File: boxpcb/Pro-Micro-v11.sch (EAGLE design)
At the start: 30 parts

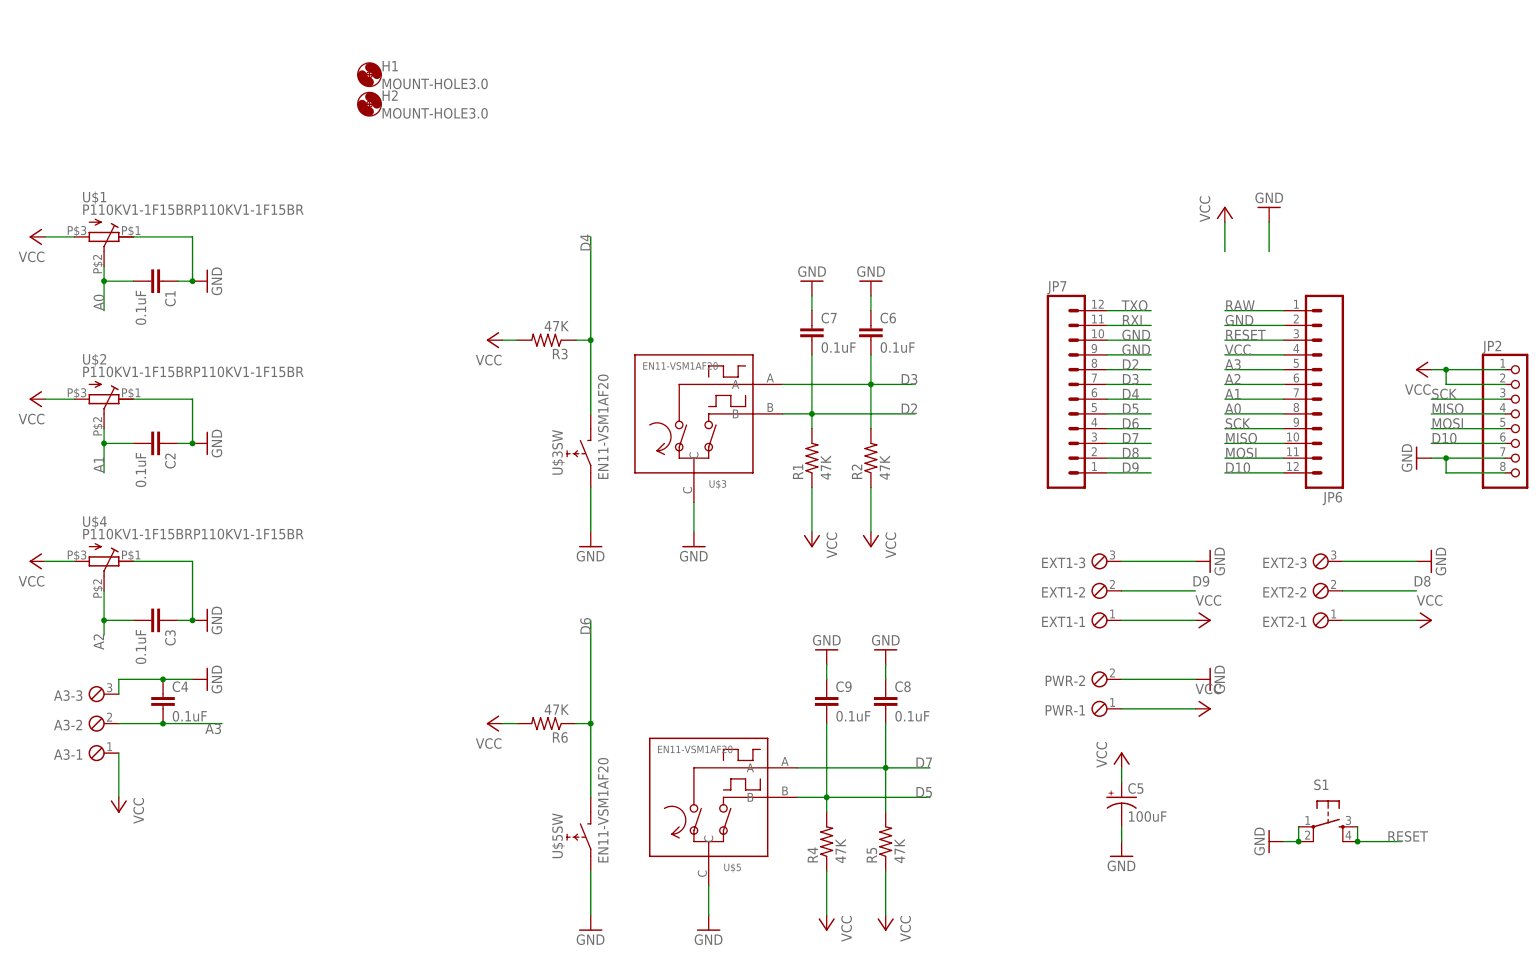
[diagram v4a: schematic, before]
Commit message: pcb simplification - remove dual rot/pot
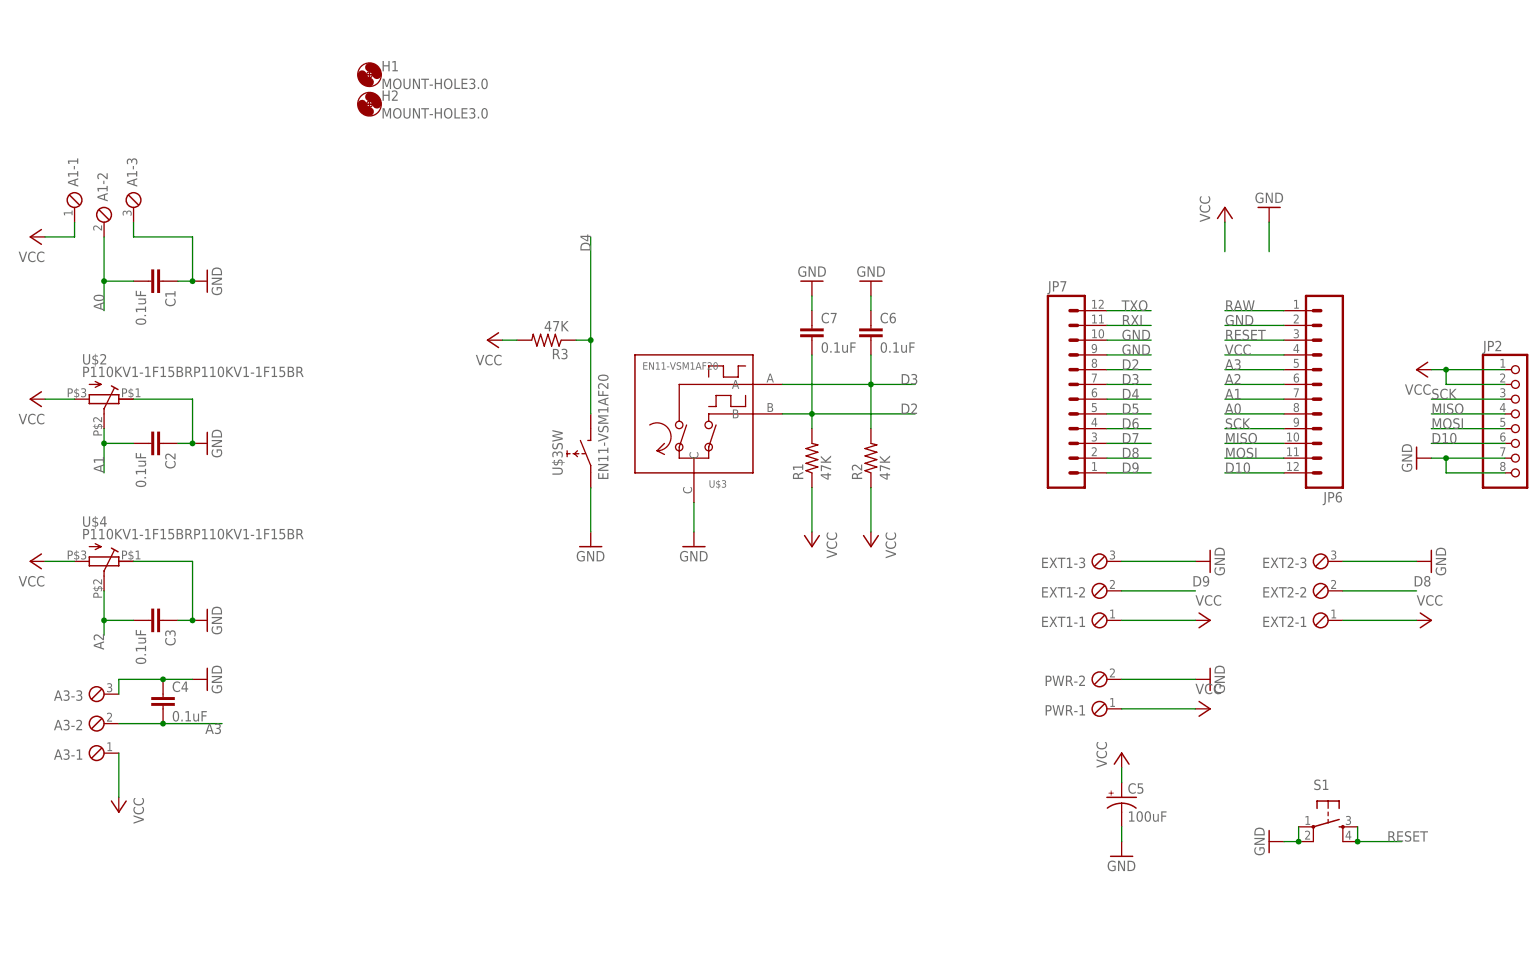
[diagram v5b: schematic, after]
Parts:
- removed C8, C9: 0.1uF, rcl:C-EU025-024X044
- removed R4, R5, R6: 47K, rcl:R-US_0204/5
- removed U$1: P110KV1-1F15BRP110KV1-1F15BR, keves:P110KV1-1F15BRP110KV1-1F15BR
- removed U$5: EN11-VSM1AF20, rotary-encoder:EN11
- added A1: (no value), con-phoenix-254:MPT3
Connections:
- net A0: now also A1-2.1; no longer U$1.S
- net D5: no longer C9.2, R4.2, U$5G$1.B
- net D6: no longer R6.1, U$5SW.E
- net D7: no longer C8.2, R5.2, U$5G$1.A
- net GND: now also A1-3.1; no longer C8.1, C9.1, U$1.A, U$5G$1.C, U$5SW.D
- net VCC: now also A1-1.1; no longer R4.1, R5.1, R6.2, U$1.E
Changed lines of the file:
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@@
 <part name="JP6" library="SparkFun" deviceset="M12" device="PTH" value=""/>
 <part name="JP7" library="SparkFun" deviceset="M12" device="PTH" value=""/>
-<part name="U$1" library="keves" deviceset="P110KV1-1F15BR" device="P110KV1-1F15BR"/>
 <part name="U$2" library="keves" deviceset="P110KV1-1F15BR" device="P110KV1-1F15BR"/>
 <part name="U$3" library="rotary-encoder" deviceset="EN11" device="" value="EN11-VSM1AF20"/>
@@
 <part name="R3" library="rcl" deviceset="R-US_" device="0204/5" value="47K"/>
 <part name="P+8" library="supply1" deviceset="VCC" device=""/>
-<part name="U$5" library="rotary-encoder" deviceset="EN11" device="" value="EN11-VSM1AF20"/>
-<part name="R4" library="rcl" deviceset="R-US_" device="0204/5" value="47K"/>
-<part name="R5" library="rcl" deviceset="R-US_" device="0204/5" value="47K"/>
-<part name="GND8" library="supply1" deviceset="GND" device=""/>
-<part name="P+9" library="supply1" deviceset="VCC" device=""/>
-<part name="P+10" library="supply1" deviceset="VCC" device=""/>
-<part name="GND9" library="supply1" deviceset="GND" device=""/>
-<part name="R6" library="rcl" deviceset="R-US_" device="0204/5" value="47K"/>
-<part name="P+11" library="supply1" deviceset="VCC" device=""/>
 <part name="EXT1" library="con-phoenix-254" deviceset="MPT3" device=""/>
 <part name="PWR" library="con-phoenix-254" deviceset="MPT2" device=""/>
@@
 <part name="C6" library="rcl" deviceset="C-EU" device="025-024X044" value="0.1uF"/>
 <part name="C7" library="rcl" deviceset="C-EU" device="025-024X044" value="0.1uF"/>
-<part name="C8" library="rcl" deviceset="C-EU" device="025-024X044" value="0.1uF"/>
-<part name="C9" library="rcl" deviceset="C-EU" device="025-024X044" value="0.1uF"/>
 <part name="GND14" library="supply1" deviceset="GND" device=""/>
 <part name="GND15" library="supply1" deviceset="GND" device=""/>
-<part name="GND16" library="supply1" deviceset="GND" device=""/>
-<part name="GND17" library="supply1" deviceset="GND" device=""/>
 <part name="S1" library="SparkFun-Electromechanical" deviceset="TAC_SWITCH" device="PTH"/>
 <part name="GND18" library="supply1" deviceset="GND" device=""/>
@@
 <part name="H1" library="holes" deviceset="MOUNT-HOLE" device="3.0"/>
 <part name="H2" library="holes" deviceset="MOUNT-HOLE" device="3.0"/>
+<part name="A1" library="con-phoenix-254" deviceset="MPT3" device=""/>
 </parts>
 <sheets>
@@
 <instance part="JP6" gate="G$1" x="241.3" y="147.32" rot="R180"/>
 <instance part="JP7" gate="G$1" x="190.5" y="149.86"/>
-<instance part="U$1" gate="G$1" x="27.94" y="175.26" rot="R270"/>
 <instance part="U$2" gate="G$1" x="27.94" y="147.32" rot="R270"/>
 <instance part="U$3" gate="G$1" x="129.54" y="144.78"/>
@@
 <instance part="R3" gate="G$1" x="104.14" y="157.48" rot="R180"/>
 <instance part="P+8" gate="VCC" x="93.98" y="157.48" rot="R90"/>
-<instance part="U$5" gate="G$1" x="132.08" y="78.74"/>
-<instance part="U$5" gate="SW" x="109.22" y="71.12" rot="R90"/>
-<instance part="R4" gate="G$1" x="152.4" y="71.12" rot="R90"/>
-<instance part="R5" gate="G$1" x="162.56" y="71.12" rot="R90"/>
-<instance part="GND8" gate="1" x="132.08" y="55.88"/>
-<instance part="P+9" gate="VCC" x="152.4" y="55.88" rot="R180"/>
-<instance part="P+10" gate="VCC" x="162.56" y="55.88" rot="R180"/>
-<instance part="GND9" gate="1" x="111.76" y="55.88"/>
-<instance part="R6" gate="G$1" x="104.14" y="91.44" rot="R180"/>
-<instance part="P+11" gate="VCC" x="93.98" y="91.44" rot="R90"/>
 <instance part="EXT1" gate="-1" x="200.66" y="109.22" rot="R180"/>
 <instance part="EXT1" gate="-2" x="200.66" y="114.3" rot="R180"/>
@@
 <instance part="C6" gate="G$1" x="160.02" y="160.02"/>
 <instance part="C7" gate="G$1" x="149.86" y="160.02"/>
-<instance part="C8" gate="G$1" x="162.56" y="96.52"/>
-<instance part="C9" gate="G$1" x="152.4" y="96.52"/>
 <instance part="GND14" gate="1" x="160.02" y="167.64" rot="R180"/>
 <instance part="GND15" gate="1" x="149.86" y="167.64" rot="R180"/>
-<instance part="GND16" gate="1" x="152.4" y="104.14" rot="R180"/>
-<instance part="GND17" gate="1" x="162.56" y="104.14" rot="R180"/>
 <instance part="S1" gate="S" x="238.76" y="73.66"/>
 <instance part="GND18" gate="1" x="228.6" y="71.12" rot="R270"/>
@@
 <instance part="H1" gate="G$1" x="73.66" y="203.2"/>
 <instance part="H2" gate="G$1" x="73.66" y="198.12"/>
+<instance part="A1" gate="-1" x="22.86" y="180.34" rot="R90"/>
+<instance part="A1" gate="-2" x="27.94" y="177.8" rot="R90"/>
+<instance part="A1" gate="-3" x="33.02" y="180.34" rot="R90"/>
 </instances>
 <busses>
@@
 <pinref part="C1" gate="G$1" pin="1"/>
 <wire x1="43.18" y1="167.64" x2="40.64" y2="167.64" width="0.1524" layer="91"/>
-<pinref part="U$1" gate="G$1" pin="A"/>
 <wire x1="33.02" y1="175.26" x2="43.18" y2="175.26" width="0.1524" layer="91"/>
 <wire x1="43.18" y1="175.26" x2="43.18" y2="167.64" width="0.1524" layer="91"/>
 <junction x="43.18" y="167.64"/>
+<pinref part="A1" gate="-3" pin="1"/>
+<wire x1="33.02" y1="175.26" x2="33.02" y2="177.8" width="0.1524" layer="91"/>
 </segment>
 <segment>
@@
 </segment>
 <segment>
-<pinref part="U$5" gate="G$1" pin="C"/>
-<pinref part="GND8" gate="1" pin="GND"/>
-<wire x1="132.08" y1="63.5" x2="132.08" y2="58.42" width="0.1524" layer="91"/>
-</segment>
-<segment>
-<pinref part="GND9" gate="1" pin="GND"/>
-<pinref part="U$5" gate="SW" pin="D"/>
-<wire x1="111.76" y1="58.42" x2="111.76" y2="66.04" width="0.1524" layer="91"/>
-</segment>
-<segment>
 <pinref part="PWR" gate="-2" pin="1"/>
 <wire x1="203.2" y1="99.06" x2="215.9" y2="99.06" width="0.1524" layer="91"/>
@@
 <pinref part="C5" gate="G$1" pin="-"/>
 <wire x1="203.2" y1="71.12" x2="203.2" y2="73.66" width="0.1524" layer="91"/>
-</segment>
-<segment>
-<pinref part="GND17" gate="1" pin="GND"/>
-<pinref part="C8" gate="G$1" pin="1"/>
-<wire x1="162.56" y1="101.6" x2="162.56" y2="99.06" width="0.1524" layer="91"/>
-</segment>
-<segment>
-<pinref part="GND16" gate="1" pin="GND"/>
-<pinref part="C9" gate="G$1" pin="1"/>
-<wire x1="152.4" y1="101.6" x2="152.4" y2="99.06" width="0.1524" layer="91"/>
 </segment>
 <segment>
@@
 </segment>
 <segment>
-<pinref part="U$1" gate="G$1" pin="E"/>
 <pinref part="P+1" gate="VCC" pin="VCC"/>
 <wire x1="22.86" y1="175.26" x2="17.78" y2="175.26" width="0.1524" layer="91"/>
+<pinref part="A1" gate="-1" pin="1"/>
+<wire x1="22.86" y1="177.8" x2="22.86" y2="175.26" width="0.1524" layer="91"/>
 </segment>
 <segment>
@@
 <pinref part="R3" gate="G$1" pin="2"/>
 <wire x1="99.06" y1="157.48" x2="96.52" y2="157.48" width="0.1524" layer="91"/>
-</segment>
-<segment>
-<pinref part="R4" gate="G$1" pin="1"/>
-<pinref part="P+9" gate="VCC" pin="VCC"/>
-<wire x1="152.4" y1="66.04" x2="152.4" y2="58.42" width="0.1524" layer="91"/>
-</segment>
-<segment>
-<pinref part="R5" gate="G$1" pin="1"/>
-<pinref part="P+10" gate="VCC" pin="VCC"/>
-<wire x1="162.56" y1="66.04" x2="162.56" y2="58.42" width="0.1524" layer="91"/>
-</segment>
-<segment>
-<pinref part="P+11" gate="VCC" pin="VCC"/>
-<pinref part="R6" gate="G$1" pin="2"/>
-<wire x1="99.06" y1="91.44" x2="96.52" y2="91.44" width="0.1524" layer="91"/>
 </segment>
 <segment>
@@
 </segment>
 <segment>
-<pinref part="U$1" gate="G$1" pin="S"/>
-<wire x1="27.94" y1="170.18" x2="27.94" y2="167.64" width="0.1524" layer="91"/>
 <label x="27.94" y="162.56" size="1.778" layer="95" rot="R90"/>
 <pinref part="C1" gate="G$1" pin="2"/>
@@
 <wire x1="33.02" y1="167.64" x2="27.94" y2="167.64" width="0.1524" layer="91"/>
 <junction x="27.94" y="167.64"/>
+<pinref part="A1" gate="-2" pin="1"/>
+<wire x1="27.94" y1="175.26" x2="27.94" y2="167.64" width="0.1524" layer="91"/>
 </segment>
 </net>
@@
 <pinref part="JP7" gate="G$1" pin="5"/>
 </segment>
-<segment>
-<pinref part="U$5" gate="G$1" pin="B"/>
-<pinref part="R4" gate="G$1" pin="2"/>
-<wire x1="147.32" y1="78.74" x2="152.4" y2="78.74" width="0.1524" layer="91"/>
-<wire x1="152.4" y1="78.74" x2="152.4" y2="76.2" width="0.1524" layer="91"/>
-<wire x1="152.4" y1="78.74" x2="170.18" y2="78.74" width="0.1524" layer="91"/>
-<junction x="152.4" y="78.74"/>
-<label x="167.64" y="78.74" size="1.778" layer="95"/>
-<pinref part="C9" gate="G$1" pin="2"/>
-<wire x1="152.4" y1="91.44" x2="152.4" y2="78.74" width="0.1524" layer="91"/>
-</segment>
 </net>
 <net name="D6" class="0">
@@
 <pinref part="JP7" gate="G$1" pin="4"/>
 </segment>
-<segment>
-<pinref part="U$5" gate="SW" pin="E"/>
-<wire x1="111.76" y1="78.74" x2="111.76" y2="91.44" width="0.1524" layer="91"/>
-<pinref part="R6" gate="G$1" pin="1"/>
-<wire x1="111.76" y1="91.44" x2="111.76" y2="109.22" width="0.1524" layer="91"/>
-<wire x1="111.76" y1="91.44" x2="109.22" y2="91.44" width="0.1524" layer="91"/>
-<junction x="111.76" y="91.44"/>
-<label x="111.76" y="106.68" size="1.778" layer="95" rot="R90"/>
-</segment>
 </net>
 <net name="D7" class="0">
@@
 <pinref part="JP7" gate="G$1" pin="3"/>
 </segment>
-<segment>
-<pinref part="U$5" gate="G$1" pin="A"/>
-<pinref part="R5" gate="G$1" pin="2"/>
-<wire x1="147.32" y1="83.82" x2="162.56" y2="83.82" width="0.1524" layer="91"/>
-<wire x1="162.56" y1="83.82" x2="162.56" y2="76.2" width="0.1524" layer="91"/>
-<wire x1="162.56" y1="83.82" x2="170.18" y2="83.82" width="0.1524" layer="91"/>
-<junction x="162.56" y="83.82"/>
-<label x="167.64" y="83.82" size="1.778" layer="95"/>
-<pinref part="C8" gate="G$1" pin="2"/>
-<wire x1="162.56" y1="91.44" x2="162.56" y2="83.82" width="0.1524" layer="91"/>
-</segment>
-</net>
+</net>

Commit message: wip
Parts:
- renumbered A1 to A2
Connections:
- net A0: now also C3.2, U$4.S; no longer A2-2.1, C1.2
- net A2: now also A2-2.1, C1.2; no longer C3.2, U$4.S
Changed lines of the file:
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@@
 <part name="H1" library="holes" deviceset="MOUNT-HOLE" device="3.0"/>
 <part name="H2" library="holes" deviceset="MOUNT-HOLE" device="3.0"/>
-<part name="A1" library="con-phoenix-254" deviceset="MPT3" device=""/>
+<part name="A2" library="con-phoenix-254" deviceset="MPT3" device=""/>
 </parts>
 <sheets>
@@
 <instance part="H1" gate="G$1" x="73.66" y="203.2"/>
 <instance part="H2" gate="G$1" x="73.66" y="198.12"/>
-<instance part="A1" gate="-1" x="22.86" y="180.34" rot="R90"/>
-<instance part="A1" gate="-2" x="27.94" y="177.8" rot="R90"/>
-<instance part="A1" gate="-3" x="33.02" y="180.34" rot="R90"/>
+<instance part="A2" gate="-1" x="22.86" y="180.34" rot="R90"/>
+<instance part="A2" gate="-2" x="27.94" y="177.8" rot="R90"/>
+<instance part="A2" gate="-3" x="33.02" y="180.34" rot="R90"/>
 </instances>
 <busses>
@@
 <wire x1="43.18" y1="175.26" x2="43.18" y2="167.64" width="0.1524" layer="91"/>
 <junction x="43.18" y="167.64"/>
-<pinref part="A1" gate="-3" pin="1"/>
+<pinref part="A2" gate="-3" pin="1"/>
 <wire x1="33.02" y1="175.26" x2="33.02" y2="177.8" width="0.1524" layer="91"/>
 </segment>
@@
 <pinref part="P+1" gate="VCC" pin="VCC"/>
 <wire x1="22.86" y1="175.26" x2="17.78" y2="175.26" width="0.1524" layer="91"/>
-<pinref part="A1" gate="-1" pin="1"/>
+<pinref part="A2" gate="-1" pin="1"/>
 <wire x1="22.86" y1="177.8" x2="22.86" y2="175.26" width="0.1524" layer="91"/>
 </segment>
@@
 </segment>
 <segment>
+<label x="27.94" y="162.56" size="1.778" layer="95" rot="R90"/>
+<pinref part="C1" gate="G$1" pin="2"/>
+<wire x1="27.94" y1="167.64" x2="27.94" y2="162.56" width="0.1524" layer="91"/>
+<wire x1="33.02" y1="167.64" x2="27.94" y2="167.64" width="0.1524" layer="91"/>
+<junction x="27.94" y="167.64"/>
+<pinref part="A2" gate="-2" pin="1"/>
+<wire x1="27.94" y1="175.26" x2="27.94" y2="167.64" width="0.1524" layer="91"/>
+</segment>
+</net>
+<net name="A1" class="0">
+<segment>
+<wire x1="231.14" y1="147.32" x2="220.98" y2="147.32" width="0.1524" layer="91"/>
+<label x="220.98" y="147.32" size="1.778" layer="95"/>
+<pinref part="JP6" gate="G$1" pin="7"/>
+</segment>
+<segment>
+<pinref part="U$2" gate="G$1" pin="S"/>
+<wire x1="27.94" y1="142.24" x2="27.94" y2="139.7" width="0.1524" layer="91"/>
+<label x="27.94" y="134.62" size="1.778" layer="95" rot="R90"/>
+<pinref part="C2" gate="G$1" pin="2"/>
+<wire x1="27.94" y1="139.7" x2="27.94" y2="134.62" width="0.1524" layer="91"/>
+<wire x1="33.02" y1="139.7" x2="27.94" y2="139.7" width="0.1524" layer="91"/>
+<junction x="27.94" y="139.7"/>
+</segment>
+</net>
+<net name="A0" class="0">
+<segment>
+<wire x1="231.14" y1="144.78" x2="220.98" y2="144.78" width="0.1524" layer="91"/>
+<label x="220.98" y="144.78" size="1.778" layer="95"/>
+<pinref part="JP6" gate="G$1" pin="8"/>
+</segment>
+<segment>
 <pinref part="U$4" gate="G$1" pin="S"/>
 <wire x1="27.94" y1="114.3" x2="27.94" y2="109.22" width="0.1524" layer="91"/>
@@
 </segment>
 </net>
-<net name="A1" class="0">
-<segment>
-<wire x1="231.14" y1="147.32" x2="220.98" y2="147.32" width="0.1524" layer="91"/>
-<label x="220.98" y="147.32" size="1.778" layer="95"/>
-<pinref part="JP6" gate="G$1" pin="7"/>
-</segment>
-<segment>
-<pinref part="U$2" gate="G$1" pin="S"/>
-<wire x1="27.94" y1="142.24" x2="27.94" y2="139.7" width="0.1524" layer="91"/>
-<label x="27.94" y="134.62" size="1.778" layer="95" rot="R90"/>
-<pinref part="C2" gate="G$1" pin="2"/>
-<wire x1="27.94" y1="139.7" x2="27.94" y2="134.62" width="0.1524" layer="91"/>
-<wire x1="33.02" y1="139.7" x2="27.94" y2="139.7" width="0.1524" layer="91"/>
-<junction x="27.94" y="139.7"/>
-</segment>
-</net>
-<net name="A0" class="0">
-<segment>
-<wire x1="231.14" y1="144.78" x2="220.98" y2="144.78" width="0.1524" layer="91"/>
-<label x="220.98" y="144.78" size="1.778" layer="95"/>
-<pinref part="JP6" gate="G$1" pin="8"/>
-</segment>
-<segment>
-<label x="27.94" y="162.56" size="1.778" layer="95" rot="R90"/>
-<pinref part="C1" gate="G$1" pin="2"/>
-<wire x1="27.94" y1="167.64" x2="27.94" y2="162.56" width="0.1524" layer="91"/>
-<wire x1="33.02" y1="167.64" x2="27.94" y2="167.64" width="0.1524" layer="91"/>
-<junction x="27.94" y="167.64"/>
-<pinref part="A1" gate="-2" pin="1"/>
-<wire x1="27.94" y1="175.26" x2="27.94" y2="167.64" width="0.1524" layer="91"/>
-</segment>
-</net>
